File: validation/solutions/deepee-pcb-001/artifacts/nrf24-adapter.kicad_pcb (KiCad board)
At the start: 2 copper layers, 30 x 25 mm, 4 parts, among them J1 Conn_01x08, J2 nRF24L01_Module

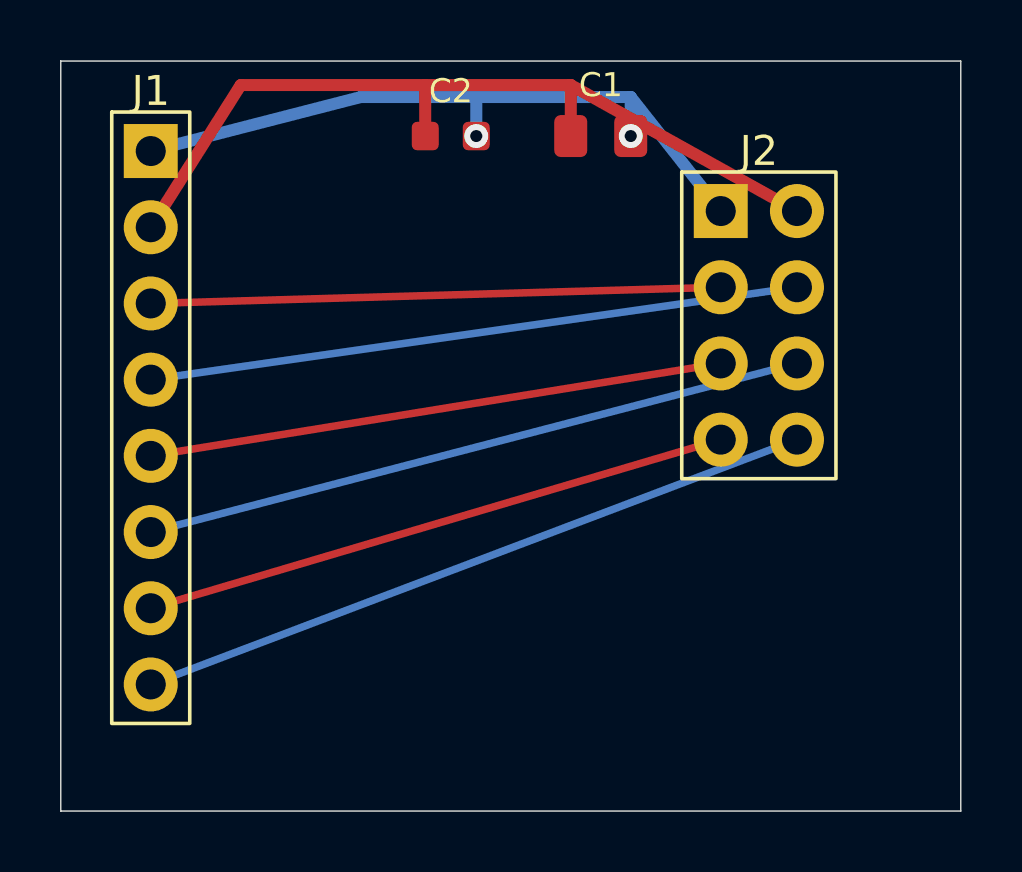
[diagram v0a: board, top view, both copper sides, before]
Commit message: feat: prepare the 48-task benchmark suite
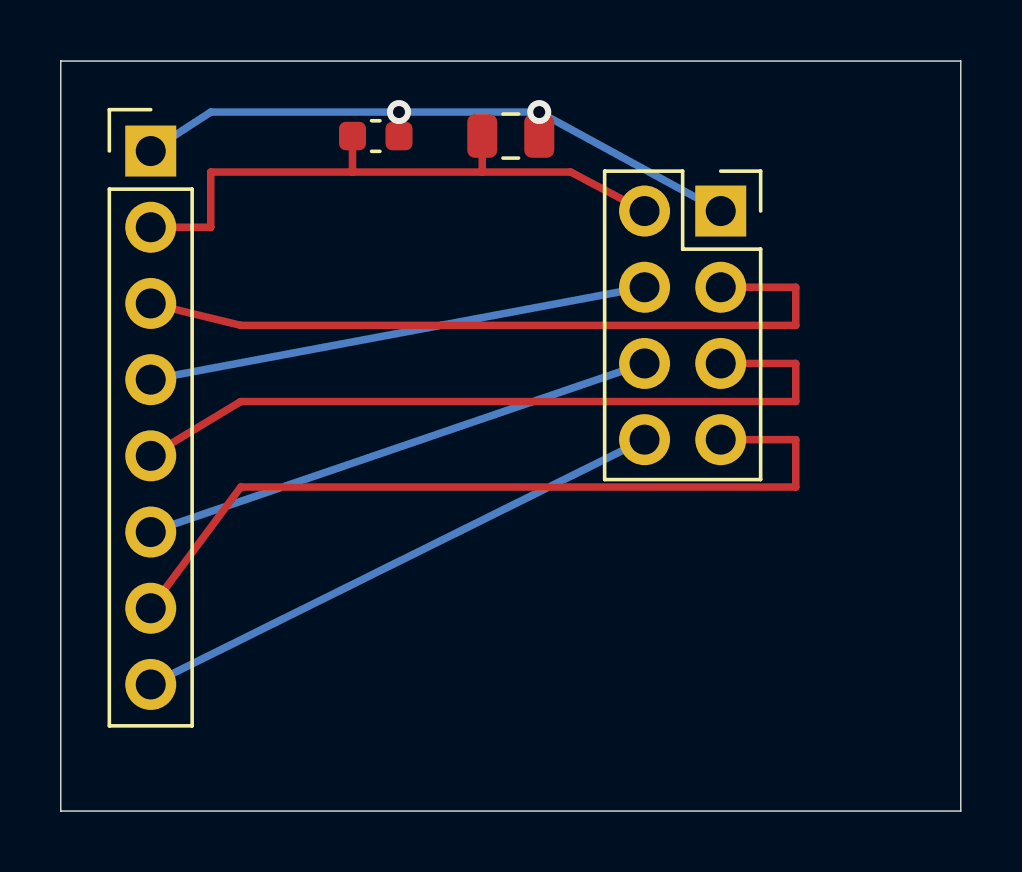
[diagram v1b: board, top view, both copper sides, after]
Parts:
- moved C1 3.00 mm to (115.0, 101.5)
- moved C2 2.50 mm to (110.5, 101.5)
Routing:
- net MISO: track 19.8 -> 27.6 mm
- net +3V3: track 28.6 -> 21.0 mm
- net SCK: track 19.2 -> 25.8 mm
- net CE: track 19.0 -> 25.4 mm
- net CSN: track 21.8 -> 16.7 mm
- net MOSI: track 22.3 -> 17.4 mm
- net IRQ: track 23.0 -> 18.4 mm
- net GND: track 23.7 -> 21.8 mm
